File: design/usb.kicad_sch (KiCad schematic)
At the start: 19 parts, among them J4 USB_B_Mini, U7 USBLC6-2SC6, U8 FT231XS

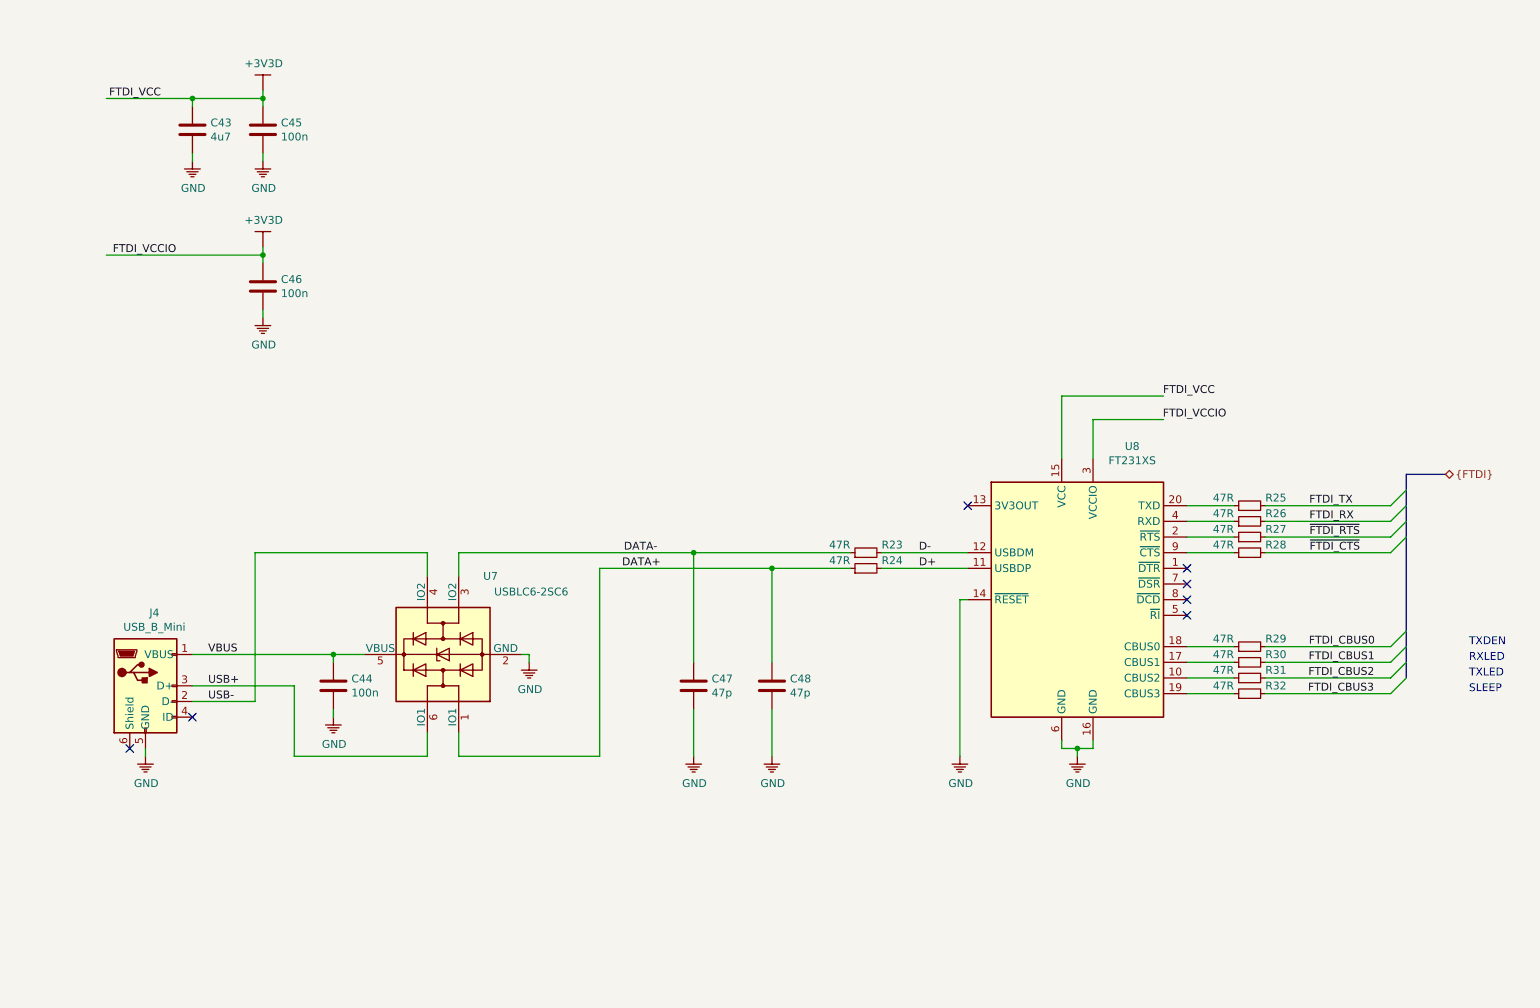
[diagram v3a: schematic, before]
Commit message: Added FTDI RST support
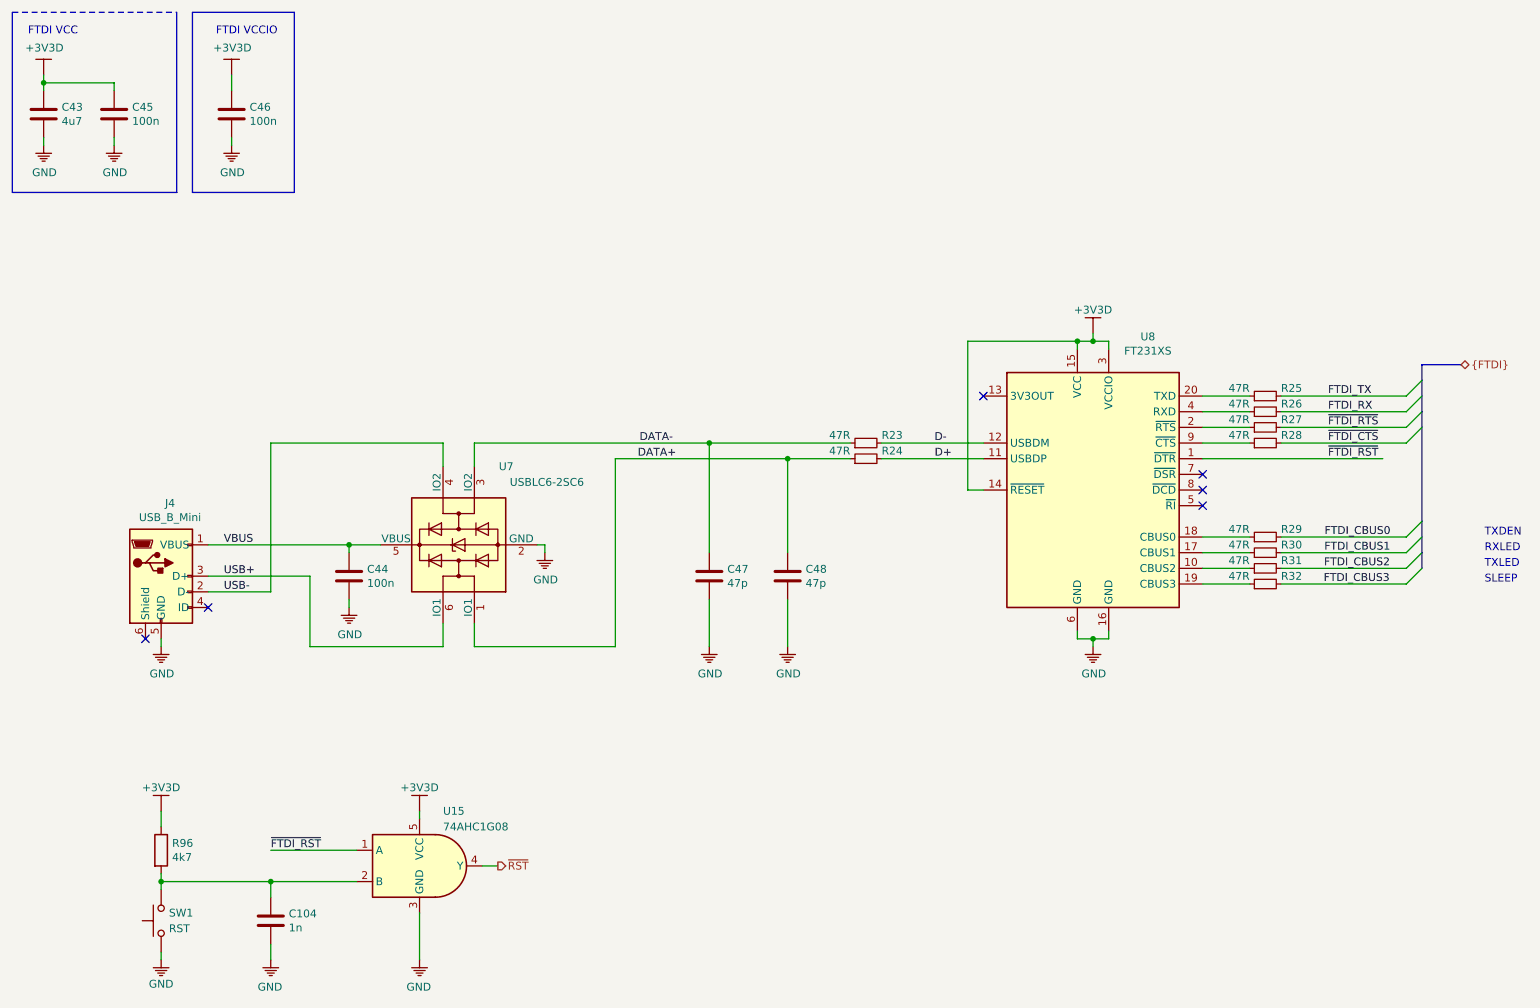
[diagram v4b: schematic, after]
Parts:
- added C104: 1n, Capacitor_SMD:C_0402_1005Metric, symbol Device:C
- added R96: 4k7, Resistor_SMD:R_0603_1608Metric, symbol Device:R
- added SW1: RST, Button_Switch_SMD:SW_SPST_CK_RS282G05A3, symbol Switch:SW_Push
- added U15: 74AHC1G08, Package_TO_SOT_SMD:SOT-23-5, symbol KLIB_Logic:74AHC1G08
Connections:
- net +3V3D: now also U8.14 (~RESET), R96.1, U15.5 (VCC)
- net GND: now also C104.2, SW1.1, U15.3 (GND); no longer U8.14 (~RESET)
- net ~FTDI_RST: now reaches U8.1 (~DTR)
- net ~FTDI_RST: now also U15.1 (A)
- new net: C104.1, R96.2, SW1.2, U15.2 (B)
- new net ~RST: U15.4 (Y)
- no-connect marks 7 -> 6
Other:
- note added: "FTDI VCC"
- note added: "FTDI VCCIO"
- moved on the sheet: C43, C44, C45, C46, C47, C48, J4, R23, R24, R25, R26, R27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

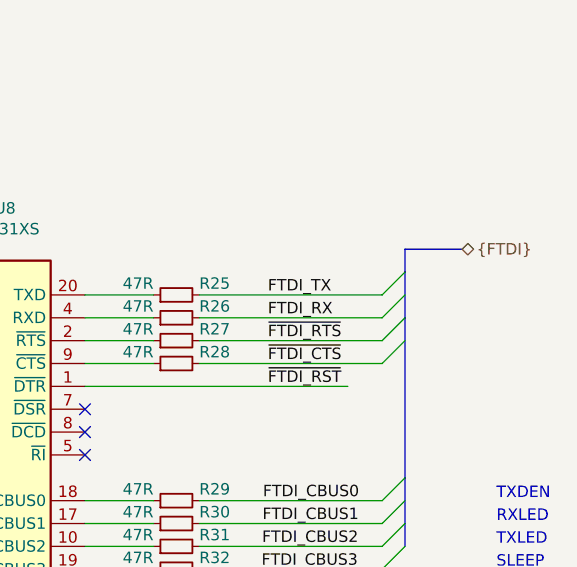
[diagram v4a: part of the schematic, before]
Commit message: Fixed MCU RST
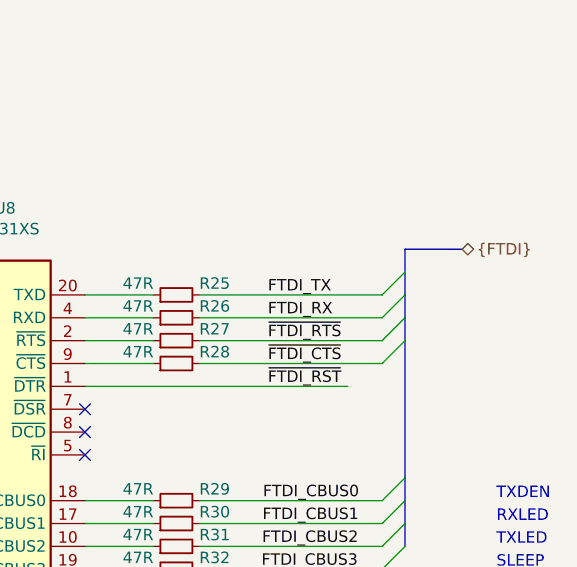
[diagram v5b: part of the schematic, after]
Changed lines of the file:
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@@
 (kicad_sch (version 20200512) (host eeschema "5.99.0-unknown-d72a778~101~ubuntu18.04.1")
-  (page 4 8)
+  (page 1 8)
   (paper "A4")
   (title_block
@@
   (junction (at 190.5 116.84))
   (no_connect (at 208.28 90.17))
+  (no_connect (at 208.28 92.71))
+  (no_connect (at 172.72 77.47))
+  (no_connect (at 36.83 116.84))
+  (no_connect (at 208.28 95.25))
   (no_connect (at 46.99 111.76))
-  (no_connect (at 172.72 77.47))
-  (no_connect (at 208.28 95.25))
-  (no_connect (at 208.28 92.71))
-  (no_connect (at 36.83 116.84))
   (bus_entry (at 241.3 77.47) (size 2.54 -2.54))
   (bus_entry (at 241.3 80.01) (size 2.54 -2.54))
@@
   (wire (pts (xy 220.98 105.41) (xy 241.3 105.41)))
   (wire (pts (xy 220.98 107.95) (xy 241.3 107.95)))
-  (bus (pts (xy 243.84 72.39) (xy 243.84 74.93)))
+  (bus (pts (xy 243.84 72.39) (xy 243.84 77.47)))
   (bus (pts (xy 243.84 72.39) (xy 250.19 72.39)))
-  (bus (pts (xy 243.84 74.93) (xy 243.84 80.01)))
+  (bus (pts (xy 243.84 77.47) (xy 243.84 80.01)))
   (bus (pts (xy 243.84 80.01) (xy 243.84 97.79)))
   (bus (pts (xy 243.84 97.79) (xy 243.84 102.87)))

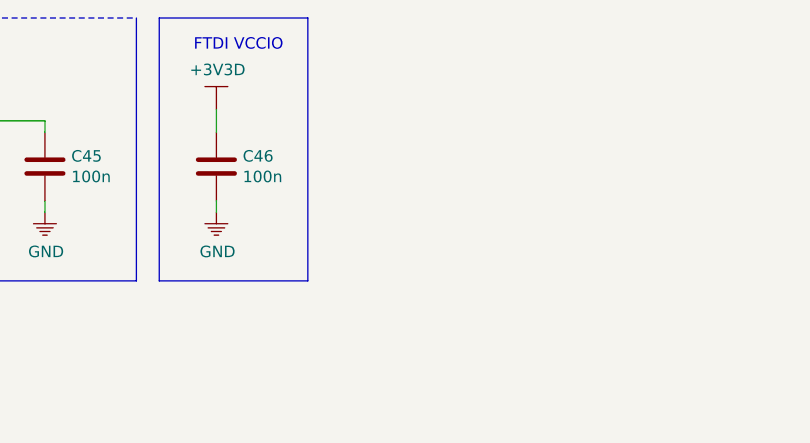
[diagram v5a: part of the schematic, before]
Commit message: Added bypass C to RST gate
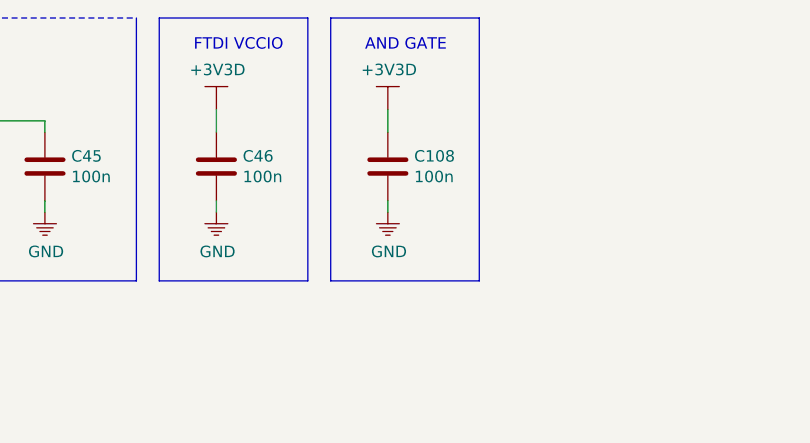
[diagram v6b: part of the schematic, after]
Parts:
- added C108: 100n, Capacitor_SMD:C_0402_1005Metric, symbol Device:C
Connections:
- net +3V3D: now also C108.1
- net GND: now also C108.2
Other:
- note added: "AND GATE"
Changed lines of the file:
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@@
 (kicad_sch (version 20200512) (host eeschema "5.99.0-unknown-d72a778~101~ubuntu18.04.1")
-  (page 1 8)
+  (page 4 8)
   (paper "A4")
   (title_block
@@
   (wire (pts (xy 63.5 106.68) (xy 63.5 118.11)))
   (wire (pts (xy 63.5 118.11) (xy 85.09 118.11)))
+  (wire (pts (xy 69.85 25.4) (xy 69.85 27.94)))
+  (wire (pts (xy 69.85 35.56) (xy 69.85 36.83)))
   (wire (pts (xy 69.85 101.6) (xy 69.85 102.87)))
   (wire (pts (xy 69.85 101.6) (xy 74.93 101.6)))
@@
   (polyline (pts (xy 44.45 44.45) (xy 60.96 44.45)))
   (polyline (pts (xy 60.96 44.45) (xy 60.96 15.24)))
+  (polyline (pts (xy 63.5 15.24) (xy 63.5 44.45)))
+  (polyline (pts (xy 63.5 15.24) (xy 80.01 15.24)))
+  (polyline (pts (xy 63.5 44.45) (xy 80.01 44.45)))
+  (polyline (pts (xy 80.01 44.45) (xy 80.01 15.24)))
   (text "FTDI VCC" (at 17.78 19.05 0)
     (effects (font (size 1.27 1.27)) (justify left bottom))
   )
   (text "FTDI VCCIO" (at 48.26 19.05 0)
+    (effects (font (size 1.27 1.27)) (justify left bottom))
+  )
+  (text "AND GATE" (at 67.31 19.05 0)
     (effects (font (size 1.27 1.27)) (justify left bottom))
   )
@@
     )
   )
+  (symbol (lib_id "KLIB_Power:+3V3D") (at 69.85 25.4 0) (unit 1)
+    (property "Reference" "#PWR071" (id 0) (at 69.85 33.02 0)
+      (effects (font (size 1.27 1.27)) hide)
+    )
+    (property "Value" "+3V3D" (id 1) (at 69.977 21.0058 0))
+    (property "Footprint" "" (id 2) (at 69.85 25.4 0)
+      (effects (font (size 1.27 1.27)) hide)
+    )
+    (property "Datasheet" "" (id 3) (at 69.85 25.4 0)
+      (effects (font (size 1.27 1.27)) hide)
+    )
+  )
+  (symbol (lib_id "KLIB_Power:GND") (at 69.85 36.83 0) (unit 1)
+    (property "Reference" "#PWR0218" (id 0) (at 69.85 41.91 0)
+      (effects (font (size 1.27 1.27)) hide)
+    )
+    (property "Value" "GND" (id 1) (at 69.977 41.2242 0))
+    (property "Footprint" "" (id 2) (at 69.85 36.83 0)
+      (effects (font (size 1.27 1.27)) hide)
+    )
+    (property "Datasheet" "" (id 3) (at 69.85 36.83 0)
+      (effects (font (size 1.27 1.27)) hide)
+    )
+  )
   (symbol (lib_id "KLIB_Power:GND") (at 69.85 111.76 0) (unit 1)
     (property "Reference" "#PWR087" (id 0) (at 69.85 116.84 0)
@@
       (effects (font (size 1.27 1.27)) hide)
     )
+  )
+  (symbol (lib_id "Device:C") (at 69.85 31.75 0) (unit 1)
+    (property "Reference" "C108" (id 0) (at 72.771 30.607 0)
+      (effects (font (size 1.27 1.27)) (justify left))
+    )
+    (property "Value" "100n" (id 1) (at 72.771 32.893 0)
+      (effects (font (size 1.27 1.27)) (justify left))
+    )
+    (property "Footprint" "Capacitor_SMD:C_0402_1005Metric" (id 2) (at 70.8152 35.56 0)
+      (effects (font (size 1.27 1.27)) hide)
+    )
+    (property "Datasheet" "~" (id 3) (at 69.85 31.75 0)
+      (effects (font (size 1.27 1.27)) hide)
+    )

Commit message: Updated some layout
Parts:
- renumbered C43 to C45, C45 to C46, C46 to C47, C104 to C48, C108 to C49, C44 to C50, C47 to C51, C48 to C52, R96 to R25, R23 to R26, R24 to R27, R25 to R28, R26 to R29, R27 to R30, R28 to R31, R29 to R32, R30 to R33, R31 to R34, R32 to R35, U15 to U7, U7 to U8, U8 to U9

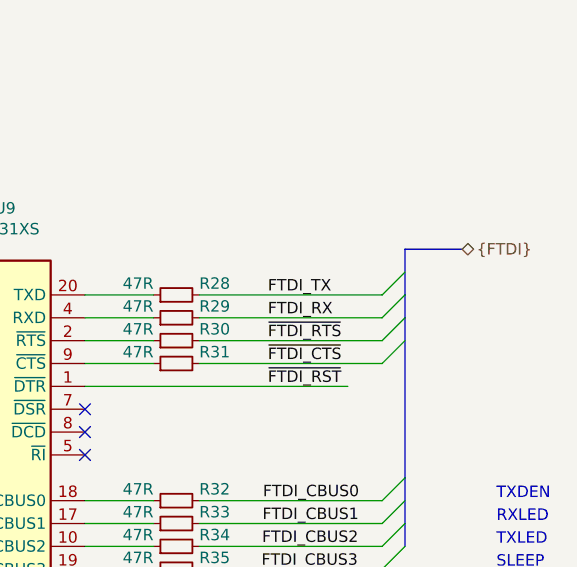
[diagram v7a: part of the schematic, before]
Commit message: Added logo and description to F.Silks
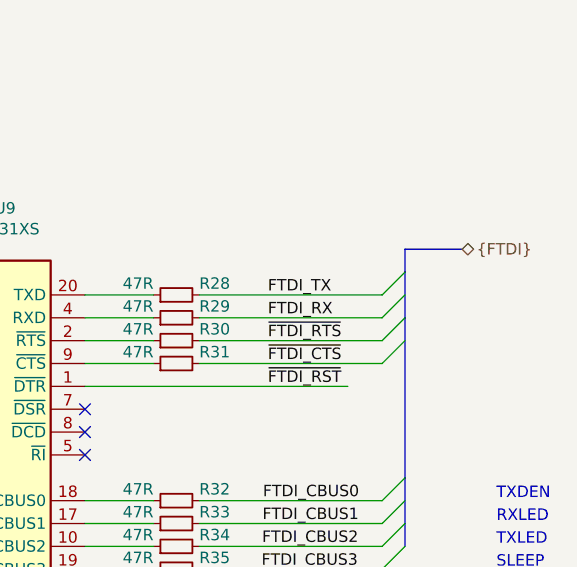
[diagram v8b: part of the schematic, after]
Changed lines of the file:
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@@
-(kicad_sch (version 20200512) (host eeschema "5.99.0-unknown-d72a778~101~ubuntu18.04.1")
+(kicad_sch (version 20200512) (host eeschema "5.99.0-unknown-4efed4b~101~ubuntu18.04.1")
   (page 4 8)
   (paper "A4")
@@
   (junction (at 190.5 68.58))
   (junction (at 190.5 116.84))
+  (no_connect (at 208.28 95.25))
   (no_connect (at 208.28 90.17))
+  (no_connect (at 46.99 111.76))
+  (no_connect (at 172.72 77.47))
   (no_connect (at 208.28 92.71))
-  (no_connect (at 172.72 77.47))
   (no_connect (at 36.83 116.84))
-  (no_connect (at 208.28 95.25))
-  (no_connect (at 46.99 111.76))
   (bus_entry (at 241.3 77.47) (size 2.54 -2.54))
   (bus_entry (at 241.3 80.01) (size 2.54 -2.54))
@@
   (wire (pts (xy 220.98 105.41) (xy 241.3 105.41)))
   (wire (pts (xy 220.98 107.95) (xy 241.3 107.95)))
-  (bus (pts (xy 243.84 72.39) (xy 243.84 77.47)))
+  (bus (pts (xy 243.84 72.39) (xy 243.84 74.93)))
   (bus (pts (xy 243.84 72.39) (xy 250.19 72.39)))
-  (bus (pts (xy 243.84 77.47) (xy 243.84 80.01)))
+  (bus (pts (xy 243.84 74.93) (xy 243.84 80.01)))
   (bus (pts (xy 243.84 80.01) (xy 243.84 97.79)))
   (bus (pts (xy 243.84 97.79) (xy 243.84 102.87)))
